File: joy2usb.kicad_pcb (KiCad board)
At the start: 2 copper layers, 55 x 90 mm, 16 parts, among them J1 DB9_Male, J2 Conn_02x04_Odd_Even, SW1 RST, SW2 SW_SPDT, U1 Arduino_Pro_Micro, U2 4066

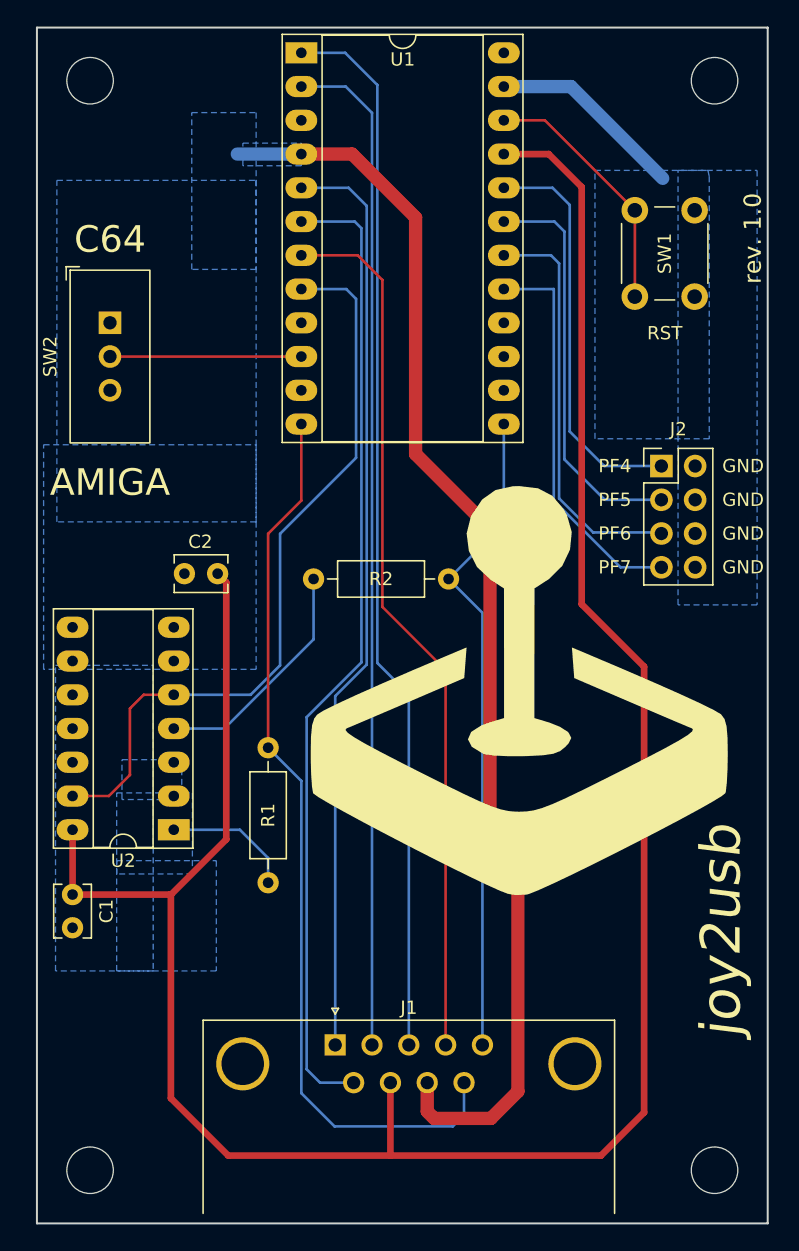
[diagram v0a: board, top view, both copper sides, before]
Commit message: PCB Rev. 2.0
Diode D1 is turned on in the same way as PULL-DOWN for the C64 Mode. Thus when D1 is on it means that PULL-DOWN for the C64 Mode is on, too.
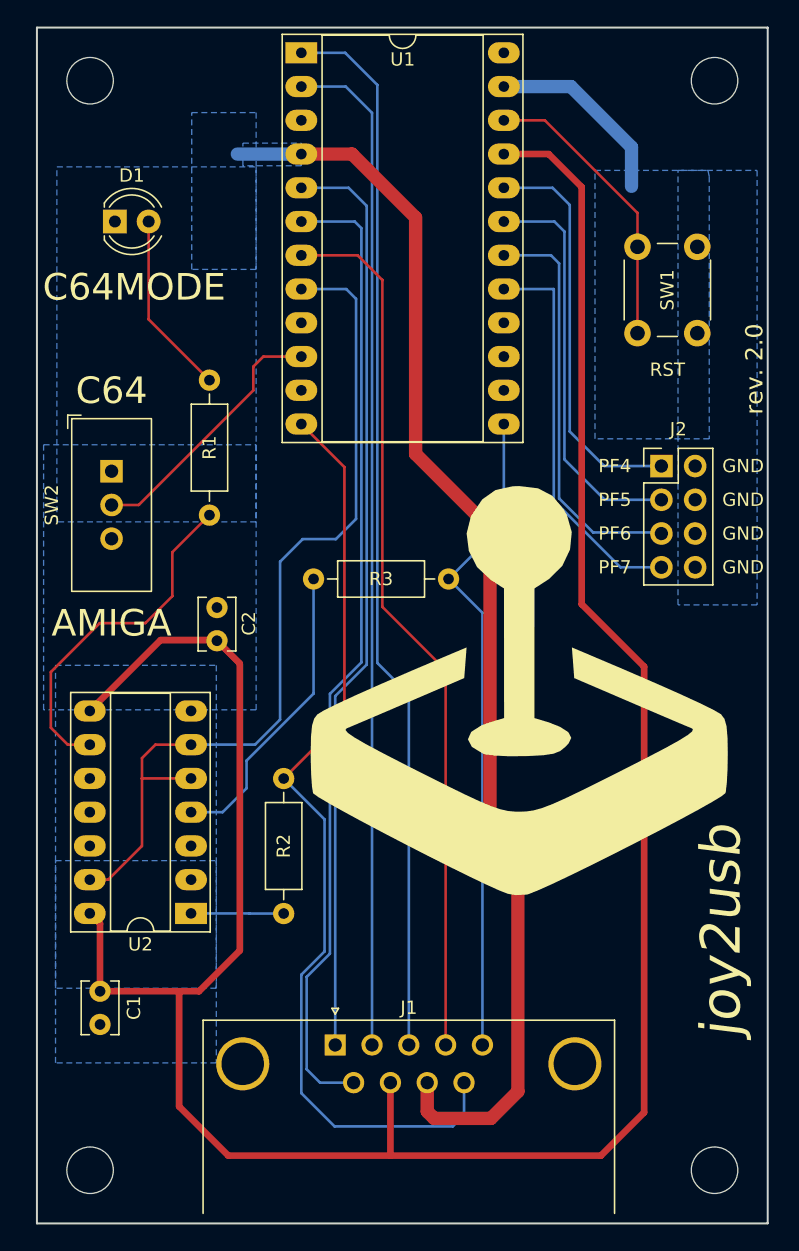
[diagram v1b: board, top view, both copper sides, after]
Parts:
- added D1: C64MODE, LED_THT:LED_D4.0mm, F.Cu at (118.9, 69.6)
- added R1: R220Ω, Resistor_THT:R_Axial_DIN0207_L6.3mm_D2.5mm_P10.16mm_Horizontal, F.Cu at (126.0, 91.7)
- moved SW2 11.2 mm to (118.6, 80.1)
- moved C1 7.57 mm to (117.8, 127.5)
- moved U2 6.43 mm to (124.6, 121.7)
- moved C2 5.05 mm to (126.5, 101.2), turned to 90 degrees
- moved SW1 2.76 mm to (158.2, 78.0)
- moved R2 2.60 mm to (131.6, 111.5)
- renumbered R1 to R2, R2 to R3
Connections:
- U2 pad 6: GND1 -> /F2F3MODE
- U2 pad 8: GND1 -> VCC
- U2 pad 9: GND1 -> Net-(R1-Pad1)
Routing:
- net Net-(R1-Pad1): track 0.00 -> 26.5 mm
- net Net-(D1-Pad2): track 0.00 -> 13.8 mm
- net /F2F3MODE: track 57.0 -> 66.8 mm
- net VCC: track 176.4 -> 184.3 mm
- net Net-(SW2-Pad2): track 14.4 -> 20.0 mm
- net Net-(R3-Pad1): track 17.8 -> 22.8 mm
- net /F2BTN: track 68.5 -> 71.8 mm
- net Net-(R2-Pad2): track 9.84 -> 6.98 mm
- net /RST: track 19.2 -> 22.0 mm
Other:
- board text added: "rev. 2.0"
- board text removed: "rev. 1.0"

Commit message: PCB Rev. 2.1
Slightly wider signal tracks and better symmetry.
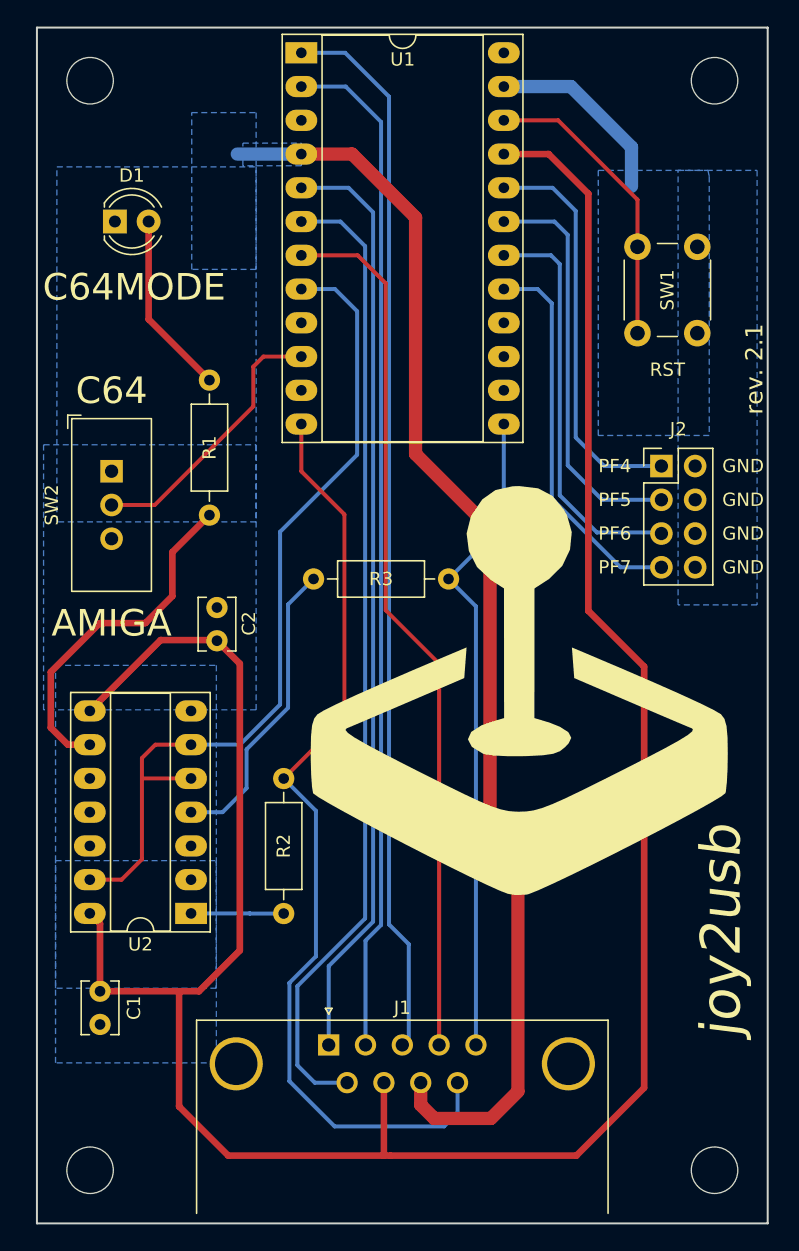
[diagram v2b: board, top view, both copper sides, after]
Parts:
- moved J1 0.49 mm to (135.0, 131.6)
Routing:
- net /F2F3MODE: track 66.8 -> 64.8 mm
- net VCC: track 184.3 -> 183.2 mm
- net /DBTN: track 76.3 -> 77.1 mm
- net /PF7: track 29.9 -> 29.1 mm
- net Net-(SW2-Pad2): track 20.0 -> 20.7 mm
- net /UBTN: track 69.6 -> 70.2 mm
- net /RST: track 22.0 -> 22.6 mm
- net /F2BTN: track 71.8 -> 71.3 mm
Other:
- board text added: "rev. 2.1"
- board text removed: "rev. 2.0"

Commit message: PCB Rev. 2.2
Bigger mass field
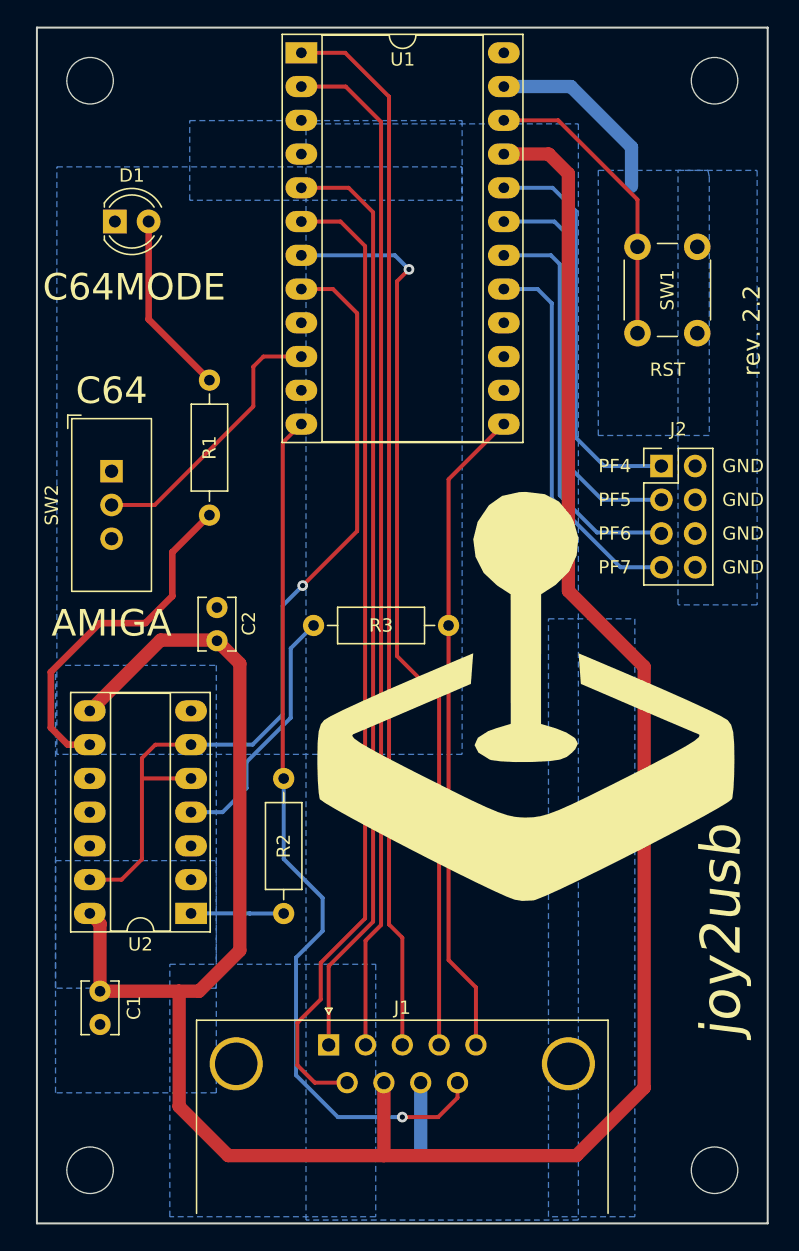
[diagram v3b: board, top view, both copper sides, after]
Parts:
- moved R3 3.50 mm to (133.8, 100.0)
- moved G*** 0.67 mm to (149.8, 105.5)
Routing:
- net GND1: track 94.6 -> 5.28 mm
- net /F2BTN: track 71.3 -> 66.9 mm, vias 0 -> 1
- net Net-(R3-Pad1): track 22.8 -> 19.3 mm
- net /RBTN: track 66.2 -> 68.6 mm, vias 0 -> 1
- net /F2F3MODE: track 64.8 -> 65.3 mm, vias 0 -> 1
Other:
- board text added: "rev. ${REVISION}"
- board text removed: "rev. 2.1"

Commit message: PCB Rev. 2.3
Update of footprints -- oval pads
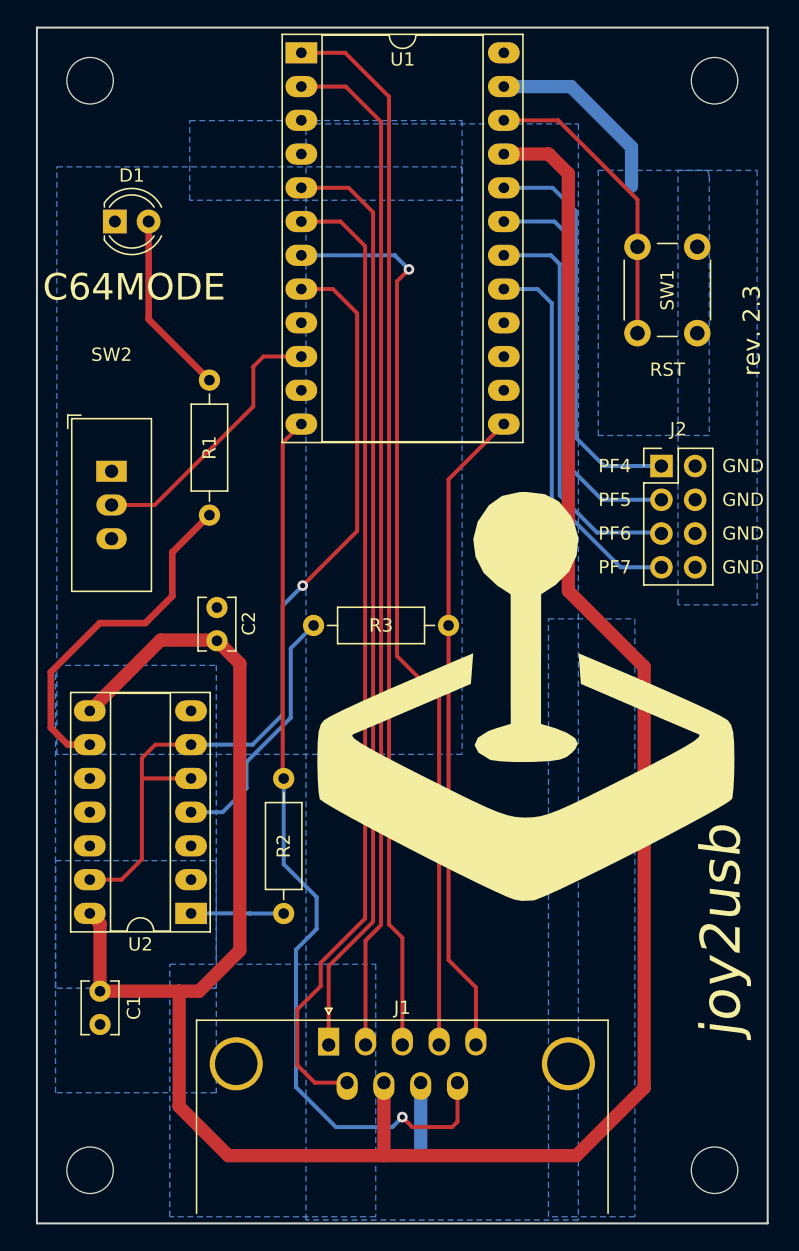
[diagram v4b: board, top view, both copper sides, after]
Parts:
- J1: footprint Connector_Dsub:DSUB-9_Male_Horizontal_P2.77x2.84mm_EdgePinOffset9.90mm_Housed_MountingHolesOffset11.32mm -> Misc:DSUB-9_Male_Horizontal_P2.77x2.84mm_EdgePinOffset9.90mm_Housed_OVAL_MountingHolesOffset11.32mm
- SW2: footprint Misc:MFP_1220_KNITTER_SWITCH_SPDT -> Misc:MFP_1220_KNITTER_SWITCH_SPDT_Oval
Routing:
- net /F2BTN: track 66.9 -> 69.2 mm
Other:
- board text added: "${TITLE}"
- board text added: "https://github.com/mistepien/${TITLE}"
- board text removed: "https://github.com/mistepien/joy2usb"
- board text removed: "joy2usb"
